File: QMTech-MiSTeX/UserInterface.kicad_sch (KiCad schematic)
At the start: 55 parts, among them CN2 U.FL-R-SMT-1(80), CN3 U.FL-R-SMT-1(80), CN4 U.FL-R-SMT-1(80), CN5 U.FL-R-SMT-1(80), CN6 U.FL-R-SMT-1(80), CN7 U.FL-R-SMT-1(80), SW1 TS-1187A-B-A-B, SW2 TS-1187A-B-A-B, SW3 TS-1187A-B-A-B, SW4 TS-1187A-B-A-B

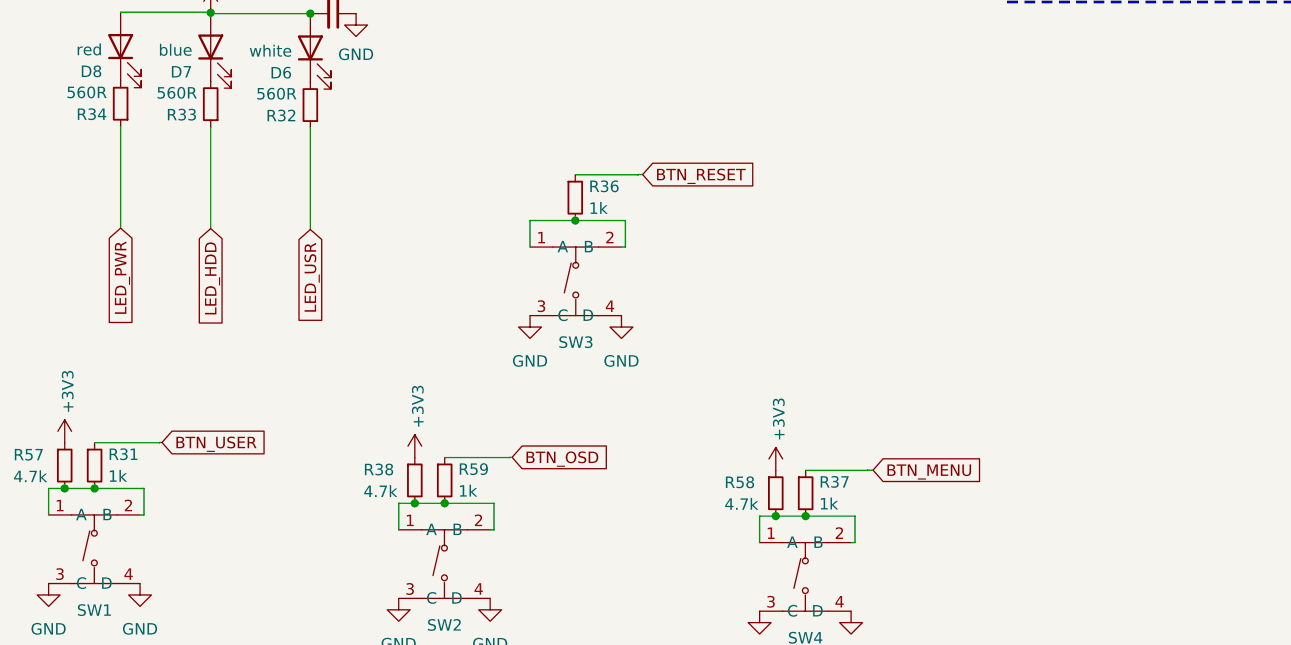
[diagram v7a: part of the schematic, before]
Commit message: use stricter design rules and cleanup all DRC errors
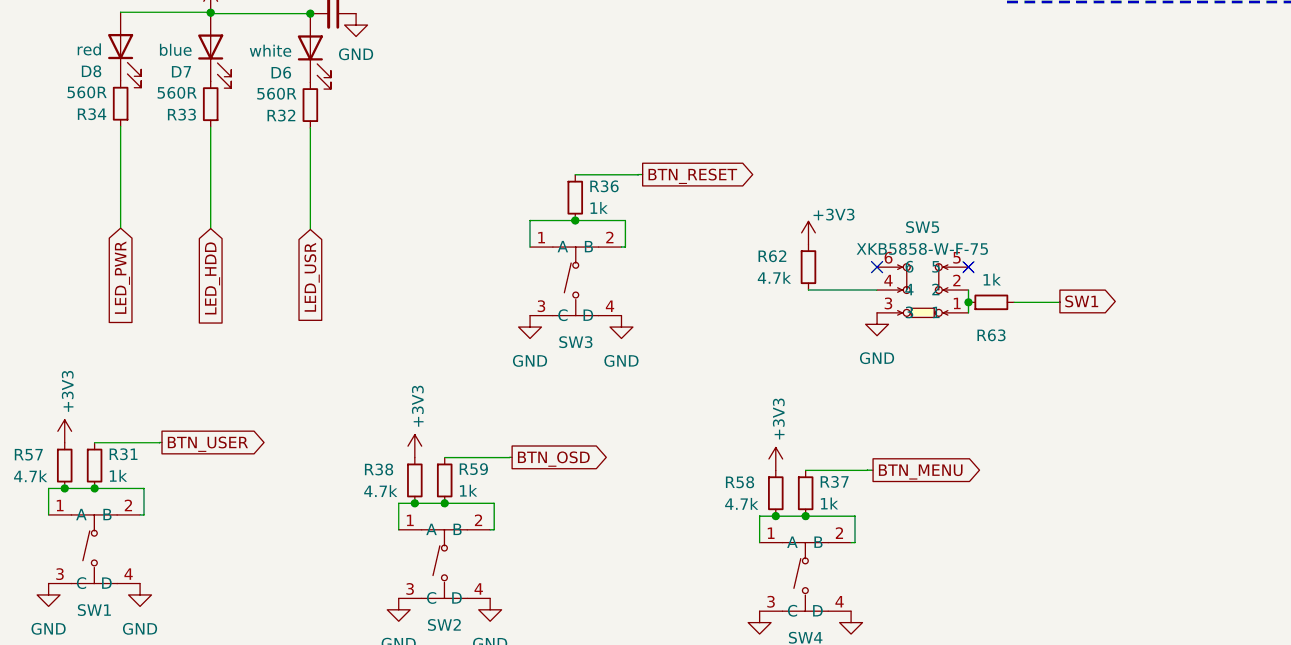
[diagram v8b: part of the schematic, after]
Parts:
- added R62: 4.7k, R_0402_1005Metric, symbol jlcpcb-basic-resistor:R_0402_4.7k
- added R63: 1k, R_0402_1005Metric, symbol jlcpcb-basic-resistor-0402:1k
- added SW5: XKB5858-W-F-75, easyeda2kicad:SW-SMD_XKB5858-W-F-75, symbol easyeda2kicad:XKB5858-W-F-75
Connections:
- net +3V3: now also R62.1
- net GND: now also SW5.3
- new net: R62.2, SW5.4
- new net: R63.1, SW5.1, SW5.2
- new net SW1: R63.2
- no-connect marks 2 -> 4
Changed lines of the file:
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@@
   (junction (at 35.0774 90.7796) (diameter 0) (color 0 0 0 0)
   )
+  (junction (at 137.16 148.6901) (diameter 0) (color 0 0 0 0)
+  )
   (junction (at 55.7022 66.7512) (diameter 0) (color 0 0 0 0)
   )
@@
   )
   (no_connect (at 35.0774 88.2396))
+  (no_connect (at 127 144.78))
   (no_connect (at 55.3974 88.2396))
+  (no_connect (at 137.16 144.78))
   (wire (pts (xy 47.5488 164.2618) (xy 47.2948 164.2618))
     (stroke (width 0) (type default))
@@
     (stroke (width 0) (type default))
   )
+  (wire (pts (xy 142.24 148.6901) (xy 147.32 148.6901))
+    (stroke (width 0) (type default))
+  )
   (wire (pts (xy 86.1958 165.9382) (xy 78.9609 165.9382))
     (stroke (width 0) (type default))
@@
     (stroke (width 0) (type default))
   )
+  (wire (pts (xy 137.16 147.32) (xy 137.16 148.6901))
+    (stroke (width 0) (type default))
+  )
   (wire (pts (xy 76.454 40.0558) (xy 85.9757 40.0558))
     (stroke (width 0) (type default))
@@
     (stroke (width 0) (type default))
   )
+  (wire (pts (xy 147.32 148.6901) (xy 147.32 148.59))
+    (stroke (width 0) (type default))
+  )
   (polyline (pts (xy 141.4526 67.5386) (xy 141.4526 115.316))
     (stroke (width 0.3) (type dot))
@@
     (stroke (width 0) (type default))
   )
+  (wire (pts (xy 137.16 148.6901) (xy 137.16 149.86))
+    (stroke (width 0) (type default))
+  )
   (wire (pts (xy 107.1118 96.1644) (xy 115.6265 96.1644))
     (stroke (width 0) (type default))
@@
     (stroke (width 0) (type default))
   )
+  (wire (pts (xy 119.38 147.32) (xy 127 147.32))
+    (stroke (width 0) (type default))
+  )
   (wire (pts (xy 26.6945 90.7796) (xy 35.0774 90.7796))
     (stroke (width 0) (type default))
@@
     )
   )
-  (global_label "BTN_OSD" (shape input) (at 86.4498 165.9128 0) (fields_autoplaced)
+  (global_label "BTN_OSD" (shape output) (at 86.4498 165.9128 0) (fields_autoplaced)
     (effects (font (size 1.27 1.27)) (justify left))
     (property "Intersheetrefs" "${INTERSHEET_REFS}" (at 97.8758 165.9128 0)
@@
     )
   )
-  (global_label "BTN_RESET" (shape input) (at 100.9566 134.493 0) (fields_autoplaced)
+  (global_label "BTN_RESET" (shape output) (at 100.9566 134.493 0) (fields_autoplaced)
+    (effects (font (size 1.27 1.27)) (justify left))
+    (property "Intersheetrefs" "${INTERSHEET_REFS}" (at 114.3177 134.493 0)
+      (effects (font (size 1.27 1.27)) (justify left))
+    )
+  )
+  (global_label "SW1" (shape output) (at 147.32 148.59 0) (fields_autoplaced)
     (effects (font (size 1.27 1.27)) (justify left))
-    (property "Intersheetrefs" "${INTERSHEET_REFS}" (at 114.2226 134.493 0)
+    (property "Intersheetrefs" "${INTERSHEET_REFS}" (at 154.2707 148.59 0)
       (effects (font (size 1.27 1.27)) (justify left))
     )
@@
     )
   )
-  (global_label "BTN_USER" (shape input) (at 47.5488 164.2618 0) (fields_autoplaced)
+  (global_label "BTN_USER" (shape output) (at 47.5488 164.2618 0) (fields_autoplaced)
     (effects (font (size 1.27 1.27)) (justify left))
-    (property "Intersheetrefs" "${INTERSHEET_REFS}" (at 60.0287 164.2618 0)
+    (property "Intersheetrefs" "${INTERSHEET_REFS}" (at 60.1238 164.2618 0)
       (effects (font (size 1.27 1.27)) (justify left))
     )
@@
     )
   )
-  (global_label "BTN_MENU" (shape input) (at 126.5557 167.3352 0) (fields_autoplaced)
+  (global_label "BTN_MENU" (shape output) (at 126.5557 167.3352 0) (fields_autoplaced)
     (effects (font (size 1.27 1.27)) (justify left))
     (property "Intersheetrefs" "${INTERSHEET_REFS}" (at 139.4331 167.3352 0)
@@
     )
   )
+  (symbol (lib_id "jlcpcb-basic-resistor:R_0402_4.7k") (at 119.38 144.78 0) (unit 1)
+    (in_bom yes) (on_board yes) (dnp no)
+    (property "Reference" "R62" (at 113.665 143.6116 0)
+      (effects (font (size 1.27 1.27)) (justify left))
+    )
+    (property "Value" "4.7k" (at 113.665 146.0358 0)
+      (effects (font (size 1.27 1.27)) (justify left))
+    )
+    (property "Footprint" "R_0402_1005Metric" (at 117.602 144.78 90)
+      (effects (font (size 1.27 1.27)) hide)
+    )
+    (property "Datasheet" "https://datasheet.lcsc.com/szlcsc/Uniroyal-Elec-0402WGF4701TCE_C25900.pdf" (at 119.38 144.78 90)
+      (effects (font (size 1.27 1.27)) hide)
+    )
+    (property "LCSC" "C25900" (at 119.38 144.78 90)
+      (effects (font (size 1.27 1.27)) hide)
+    )
+    (pin "2")
+    (pin "1")
+    (instances
+      (project "QMTech-MiSTeX"
+        (path "/bf95850e-2fcb-4784-a603-f17fc357556b/cce2b405-ae09-44af-ba42-d113d6ffe521"
+          (reference "R62") (unit 1)
+        )
+      )
+    )
+  )
   (symbol (lib_id "power:GND") (at 34.9504 179.9336 0) (unit 1)
     (in_bom yes) (on_board yes) (dnp no) (fields_autoplaced)
@@
     )
   )
+  (symbol (lib_id "power:GND") (at 127 149.86 0) (unit 1)
+    (in_bom yes) (on_board yes) (dnp no) (fields_autoplaced)
+    (property "Reference" "#PWR0184" (at 127 156.21 0)
+      (effects (font (size 1.27 1.27)) hide)
+    )
+    (property "Value" "GND" (at 127 154.94 0)
+      (effects (font (size 1.27 1.27)))
+    )
+    (property "Footprint" "" (at 127 149.86 0)
+      (effects (font (size 1.27 1.27)) hide)
+    )
+    (property "Datasheet" "" (at 127 149.86 0)
+      (effects (font (size 1.27 1.27)) hide)
+    )
+    (pin "1")
+    (instances
+      (project "QMTech-MiSTeX"
+        (path "/bf95850e-2fcb-4784-a603-f17fc357556b/cce2b405-ae09-44af-ba42-d113d6ffe521"
+          (reference "#PWR0184") (unit 1)
+        )
+      )
+    )
+  )
   (symbol (lib_id "easyeda2kicad:U-A-39WD-W-1") (at 62.484 42.5958 0) (mirror y) (unit 1)
     (in_bom yes) (on_board yes) (dnp no)
@@
     )
   )
+  (symbol (lib_id "jlcpcb-basic-resistor-0402:1k") (at 139.7 148.6901 90) (unit 1)
+    (in_bom yes) (on_board yes) (dnp no)
+    (property "Reference" "R63" (at 139.7 152.4 90)
+      (effects (font (size 1.27 1.27)))
+    )
+    (property "Value" "1k" (at 139.7 146.2334 90)
+      (effects (font (size 1.27 1.27)))
+    )
+    (property "Footprint" "R_0402_1005Metric" (at 139.7 150.4681 90)
+      (effects (font (size 1.27 1.27)) hide)
+    )
+    (property "Datasheet" "https://datasheet.lcsc.com/szlcsc/Uniroyal-Elec-0402WGF1001TCE_C11702.pdf" (at 139.7 148.6901 90)
+      (effects (font (size 1.27 1.27)) hide)
+    )
+    (property "LCSC" "C11702" (at 139.7 148.6901 90)
+      (effects (font (size 1.27 1.27)) hide)
+    )
+    (pin "2")
+    (pin "1")
+    (instances
+      (project "QMTech-MiSTeX"
+        (path "/bf95850e-2fcb-4784-a603-f17fc357556b/cce2b405-ae09-44af-ba42-d113d6ffe521"
+          (reference "R63") (unit 1)
+        )
+      )
+    )
+  )
   (symbol (lib_id "jlcpcb-basic-resistor-0402:1k") (at 229.87 89.4334 90) (unit 1)
     (in_bom yes) (on_board yes) (dnp no) (fields_autoplaced)
@@
     )
   )
+  (symbol (lib_id "power:+3V3") (at 119.38 142.24 0) (unit 1)
+    (in_bom yes) (on_board yes) (dnp no)
+    (property "Reference" "#PWR0181" (at 119.38 146.05 0)
+      (effects (font (size 1.27 1.27)) hide)
+    )
+    (property "Value" "+3V3" (at 119.761 138.9888 0)
+      (effects (font (size 1.27 1.27)) (justify left))
+    )
+    (property "Footprint" "" (at 119.38 142.24 0)
+      (effects (font (size 1.27 1.27)) hide)
+    )
+    (property "Datasheet" "" (at 119.38 142.24 0)
+      (effects (font (size 1.27 1.27)) hide)
+    )
+    (pin "1")
+    (instances
+      (project "QMTech-MiSTeX"
+        (path "/bf95850e-2fcb-4784-a603-f17fc357556b/cce2b405-ae09-44af-ba42-d113d6ffe521"
+          (reference "#PWR0181") (unit 1)
+        )
+      )
+    )
+  )
   (symbol (lib_id "jlcpcb-basic-resistor:R_0402_4.7k") (at 75.6412 168.4782 0) (unit 1)
     (in_bom yes) (on_board yes) (dnp no)
@@
         )
       )
+    )
+  )
+  (symbol (lib_id "easyeda2kicad:XKB5858-W-F-75") (at 132.08 147.32 90) (unit 1)
+    (in_bom yes) (on_board yes) (dnp no) (fields_autoplaced)
+    (property "Reference" "SW5" (at 132.08 140.3827 90)
+      (effects (font (size 1.27 1.27)))
+    )
+    (property "Value" "XKB5858-W-F-75" (at 132.08 142.8069 90)
+      (effects (font (size 1.27 1.27)))
+    )
+    (property "Footprint" "easyeda2kicad:SW-SMD_XKB5858-W-F-75" (at 144.78 147.32 0)
+      (effects (font (size 1.27 1.27)) hide)
+    )
+    (property "Datasheet" "https://lcsc.com/product-detail/Electrical-Switches_XKB-Connectivity-XKB5858-W-F-75_C780037.html" (at 147.32 147.32 0)
+      (effects (font (size 1.27 1.27)) hide)
+    )
+    (property "LCSC Part" "C780037" (at 149.86 147.32 0)
+      (effects (font (size 1.27 1.27)) hide)
+    )
+    (pin "2")
+    (pin "1")
+    (pin "4")
+    (pin "5")
+    (pin "3")
+    (pin "6")
+    (instances
+      (project "QMTech-MiSTeX"
+        (path "/bf95850e-2fcb-4784-a603-f17fc357556b/cce2b405-ae09-44af-ba42-d113d6ffe521"
+          (reference "SW5") (unit 1)
+        )
+      )
